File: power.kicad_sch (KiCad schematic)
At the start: 36 parts, among them J1 USB_C_Receptacle_USB2.0_14P, J8 Conn_01x04, J9 Conn_01x04, U10 TPS6282x, U4 TPS6282x

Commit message: schem: reannotate
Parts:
- renumbered C28 to C24, C2 to C25, C16 to C26, C29 to C27, C4 to C28, C36 to C29, C19 to C30, C37 to C31, C26 to C32, C38 to C33, C27 to C34, C39 to C35, D7 to D3, D8 to D4, D3 to D5, D4 to D6, D6 to D7, D9 to D8, J1 to J3, J8 to J4, J9 to J5, L2 to L4, L1 to L5, R3 to R15, R4 to R16, R14 to R17, R8 to R18, R15 to R19, R6 to R20, R16 to R21, TP7 to TP4, TP6 to TP5, TP8 to TP6, TP9 to TP7, U4 to U11

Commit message: schem: update footprints to glcs
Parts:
- L4, L5: footprint Pers:TDK_TFM201610ALC -> GLCS:TDK_TFM201610ALC
- U10, U11: footprint Pers:Texas_VSON-6_1.5x1.5mm_P0.5mm_DMQ0006A -> GLCS:Texas_VSON-6_1.5x1.5mm_P0.5mm_DMQ0006A
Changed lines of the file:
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@@
 			)
 		)
-		(property "Footprint" "Pers:TDK_TFM201610ALC"
+		(property "Footprint" "GLCS:TDK_TFM201610ALC"
 			(at 201.93 107.95 0)
 			(hide yes)
@@
 			)
 		)
-		(property "Footprint" "Pers:Texas_VSON-6_1.5x1.5mm_P0.5mm_DMQ0006A"
+		(property "Footprint" "GLCS:Texas_VSON-6_1.5x1.5mm_P0.5mm_DMQ0006A"
 			(at 193.04 87.63 0)
 			(hide yes)
@@
 			)
 		)
-		(property "Footprint" "Pers:TDK_TFM201610ALC"
+		(property "Footprint" "GLCS:TDK_TFM201610ALC"
 			(at 201.93 71.12 0)
 			(hide yes)
@@
 			)
 		)
-		(property "Footprint" "Pers:Texas_VSON-6_1.5x1.5mm_P0.5mm_DMQ0006A"
+		(property "Footprint" "GLCS:Texas_VSON-6_1.5x1.5mm_P0.5mm_DMQ0006A"
 			(at 193.04 124.46 0)
 			(hide yes)

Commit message: schem: fix can net labels
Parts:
- removed D4: SMBJ6.0CA, Diode_SMD:D_SMB, symbol Device:D_TVS
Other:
- moved on the sheet: D3

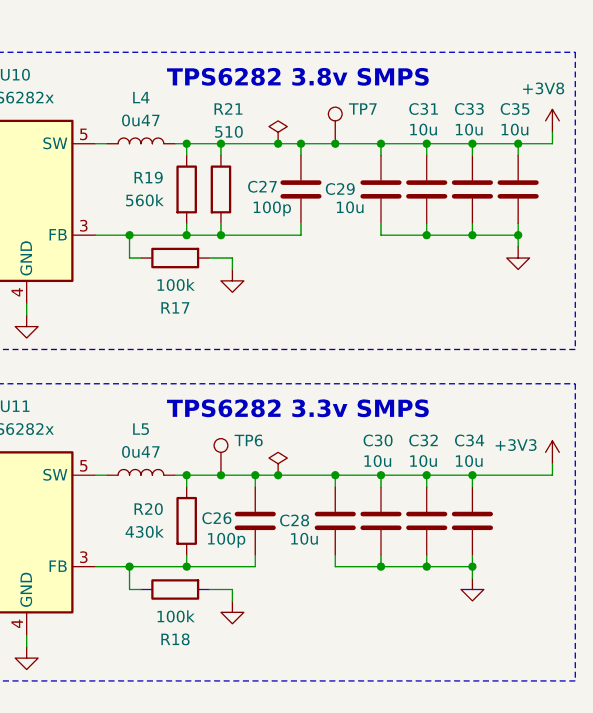
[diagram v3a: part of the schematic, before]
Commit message: schem: update 10u caps to 0603
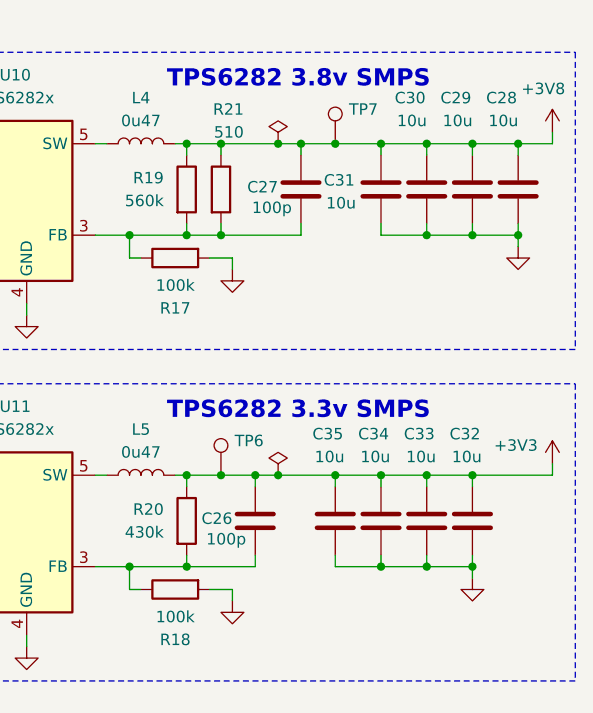
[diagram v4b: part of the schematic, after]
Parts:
- C28, C29, C30, C31, C32, C33, C34, C35: footprint Capacitor_SMD:C_0402_1005Metric -> Capacitor_SMD:C_0603_1608Metric; JLCPCB Part # C15525 -> C19702; Manufacturer Part Number CL05A106MQ5NUNC -> CL10A106KP8NNNC
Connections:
- net +3V3: now also C33.1, C35.1; no longer C28.1, C30.1
- net +3V8: now also C28.1, C30.1; no longer C33.1, C35.1

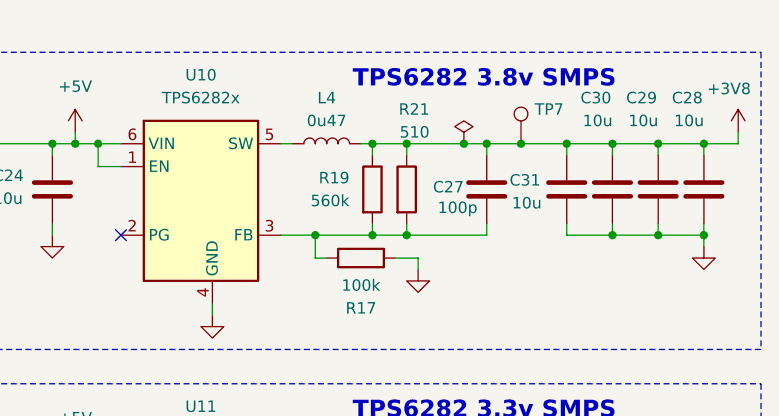
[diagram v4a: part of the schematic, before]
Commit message: pcb: add SMPSs layout
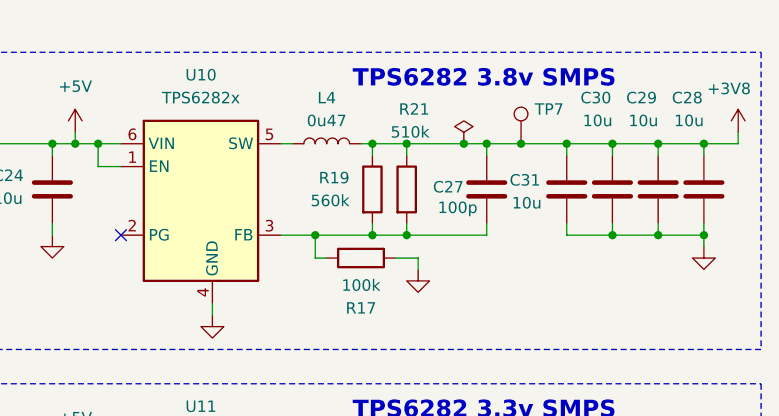
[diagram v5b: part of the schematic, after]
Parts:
- R21: value 510 -> 510k
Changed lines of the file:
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@@
 			)
 		)
-		(property "Value" "510"
+		(property "Value" "510k"
 			(at 213.36 69.85 0)
 			(show_name no)

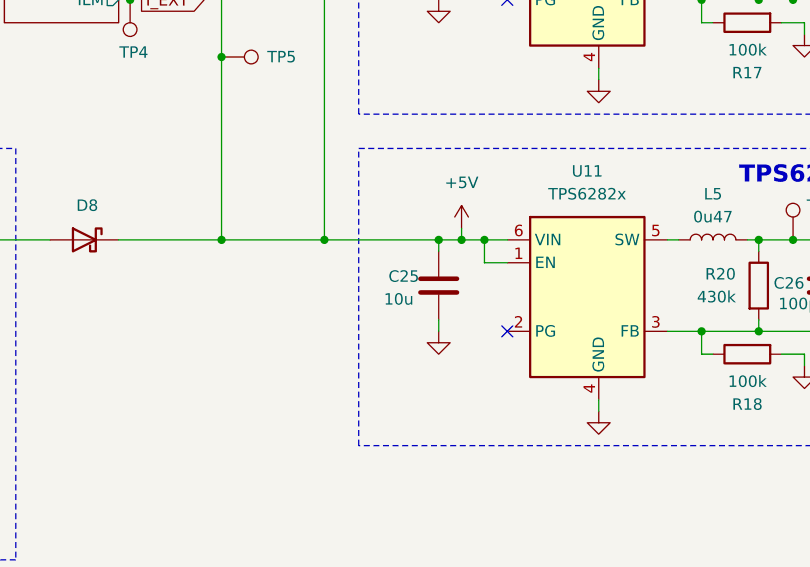
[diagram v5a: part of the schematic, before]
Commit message: pcb: add laser & tft layout
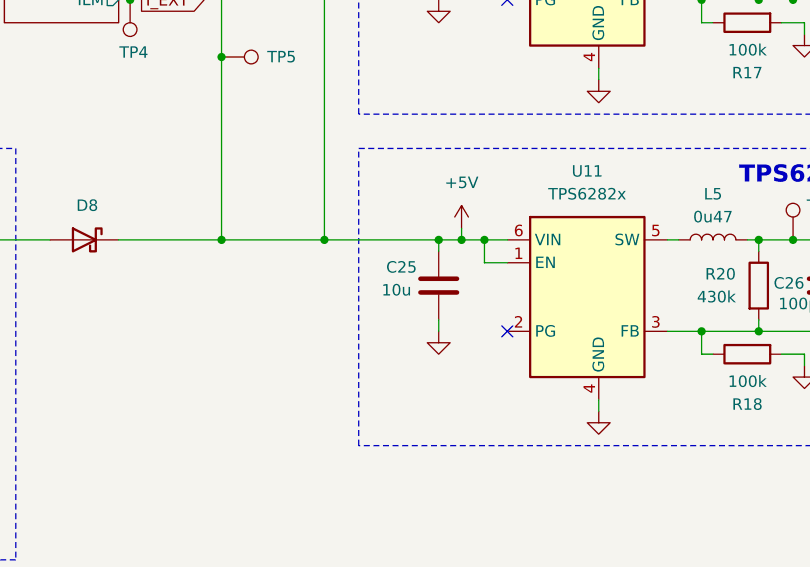
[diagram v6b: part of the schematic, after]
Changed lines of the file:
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@@
 		(dnp no)
 		(property "Reference" "C25"
-			(at 165.862 112.014 0)
+			(at 165.608 110.998 0)
 			(show_name no)
 			(do_not_autoplace no)
@@
 		)
 		(property "Value" "10u"
-			(at 165.354 114.554 0)
+			(at 165.1 113.538 0)
 			(show_name no)
 			(do_not_autoplace no)
